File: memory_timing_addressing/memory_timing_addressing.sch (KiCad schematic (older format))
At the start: 1 part, among them P1 DIN_41612_128P

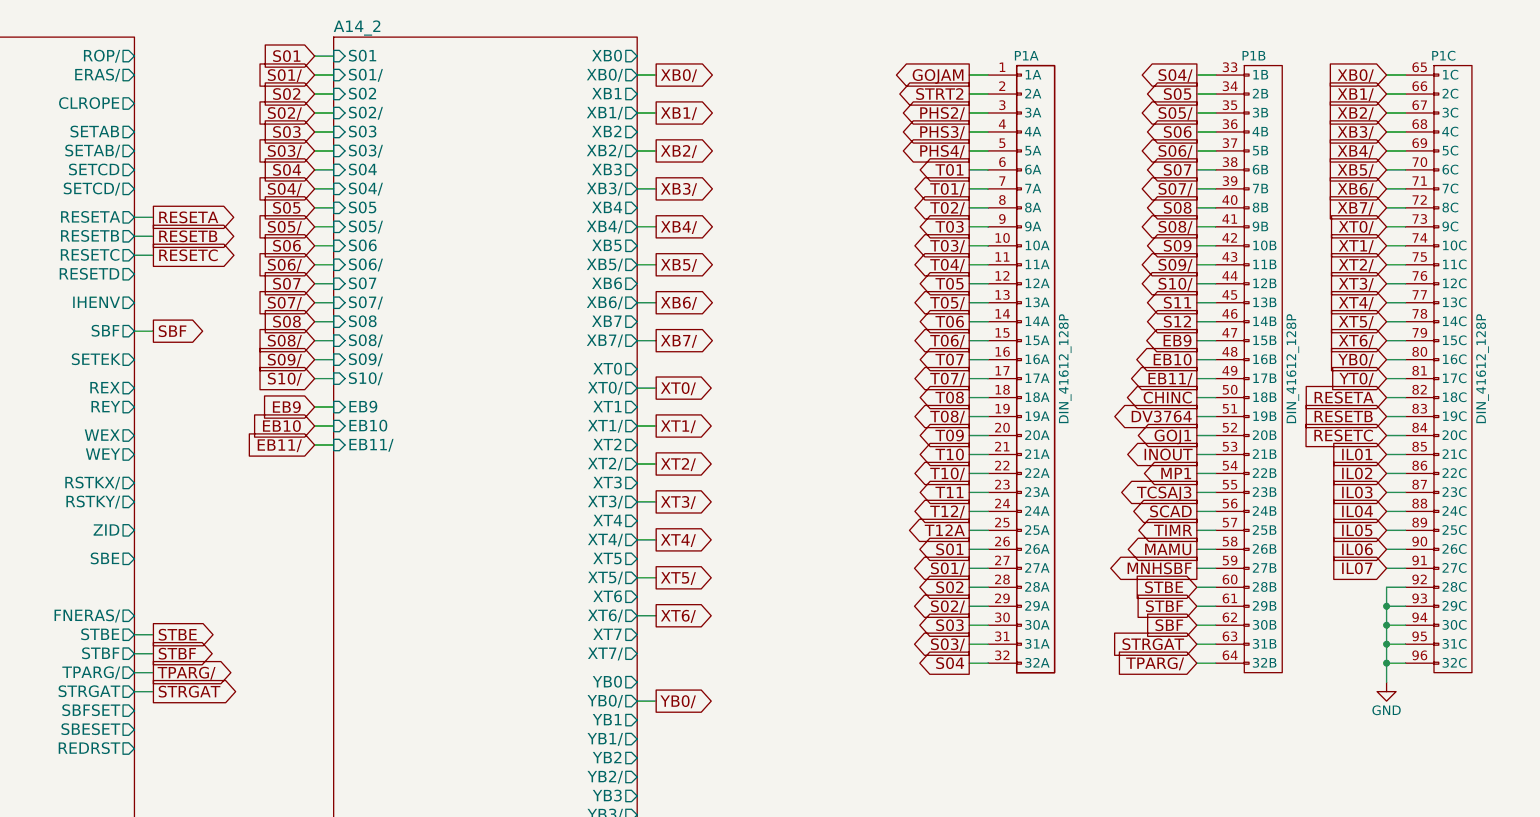
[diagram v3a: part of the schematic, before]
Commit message: Updated fixed memory model, plus various bugfixes
Rope memory control signals are now decoded much earlier in the cycle to
determine the target address, allowing slower memory devices (such as
the EPCS on the DE0 Nano) enough time to load their data.

The bugfixes are mostly wiring errors discovered by debugging lockups in
when running Colossus 237 -- all were causing the ST2 pulse to not
occur, so errors that *don't* prevent ST2 from happening very well might
be present in the instructions that have been fixed.

The computer now gets through the initialization code and enters an
infinite loop when attempting to invoke the interpeter, due to the lack
of erasable memory.
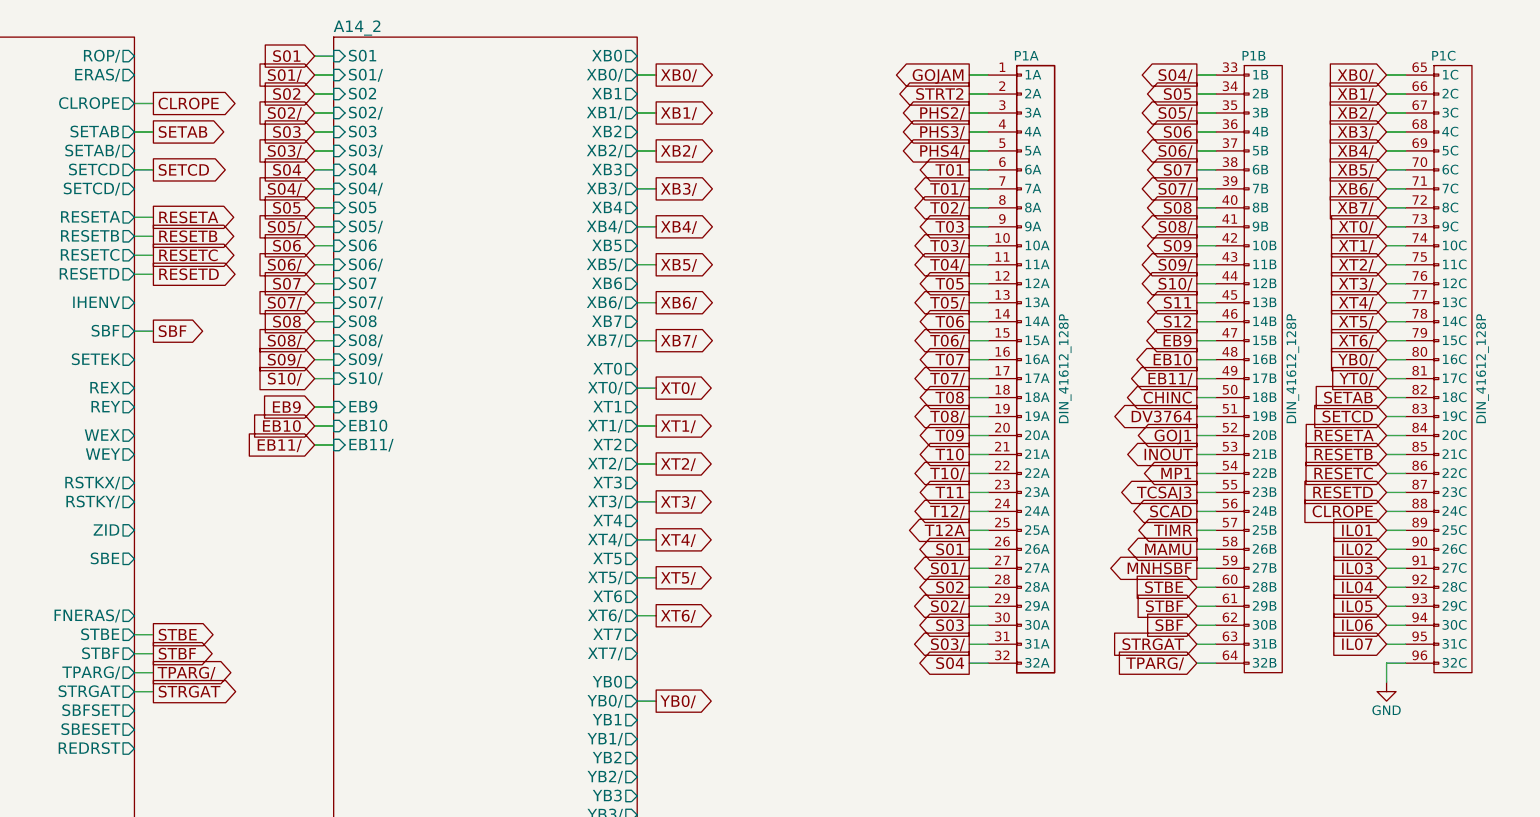
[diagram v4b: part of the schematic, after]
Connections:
- net GND: no longer P1.92 (28C), P1.93 (29C), P1.94 (30C), P1.95 (31C)
- net IL01: now also P1.89 (25C); no longer P1.85 (21C)
- net IL02: now also P1.90 (26C); no longer P1.86 (22C)
- net IL03: now also P1.91 (27C); no longer P1.87 (23C)
- net IL04: now also P1.92 (28C); no longer P1.88 (24C)
- net IL05: now also P1.93 (29C); no longer P1.89 (25C)
- net IL06: now also P1.94 (30C); no longer P1.90 (26C)
- net IL07: now also P1.95 (31C); no longer P1.91 (27C)
- net RESETA: now also P1.84 (20C); no longer P1.82 (18C)
- net RESETB: now also P1.85 (21C); no longer P1.83 (19C)
- net RESETC: now also P1.86 (22C); no longer P1.84 (20C)
- new net CLROPE: P1.88 (24C)
- new net RESETD: P1.87 (23C)
- new net SETAB: P1.82 (18C)
- new net SETCD: P1.83 (19C)
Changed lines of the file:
@@
 $EndComp
 Wire Wire Line
-	9450 4100 9550 4100
-Wire Wire Line
-	9450 4200 9550 4200
-Connection ~ 9450 4200
-Wire Wire Line
-	9450 4300 9550 4300
-Connection ~ 9450 4300
-Wire Wire Line
-	9450 4400 9550 4400
-Connection ~ 9450 4400
-Wire Wire Line
 	9450 4500 9550 4500
-Connection ~ 9450 4500
 $Comp
 L GND #PWR01
@@
 RESETC
 Wire Wire Line
-	9550 3100 9450 3100
-Text GLabel 9450 3100 0    60   Input ~ 0
-RESETA
-Wire Wire Line
-	9550 3200 9450 3200
-Text GLabel 9450 3200 0    60   Input ~ 0
-RESETB
-Wire Wire Line
 	9550 3300 9450 3300
 Text GLabel 9450 3300 0    60   Input ~ 0
+RESETA
+Wire Wire Line
+	9550 3400 9450 3400
+Text GLabel 9450 3400 0    60   Input ~ 0
+RESETB
+Wire Wire Line
+	9550 3500 9450 3500
+Text GLabel 9450 3500 0    60   Input ~ 0
 RESETC
 Wire Wire Line
@@
 IL07
 Wire Wire Line
-	9550 3400 9450 3400
-Text GLabel 9450 3400 0    60   Input ~ 0
-IL01
-Wire Wire Line
-	9550 3500 9450 3500
-Text GLabel 9450 3500 0    60   Input ~ 0
-IL02
-Wire Wire Line
-	9550 3600 9450 3600
-Text GLabel 9450 3600 0    60   Input ~ 0
-IL03
-Wire Wire Line
-	9550 3700 9450 3700
-Text GLabel 9450 3700 0    60   Input ~ 0
-IL04
-Wire Wire Line
 	9550 3800 9450 3800
 Text GLabel 9450 3800 0    60   Input ~ 0
-IL05
+IL01
 Wire Wire Line
 	9550 3900 9450 3900
 Text GLabel 9450 3900 0    60   Input ~ 0
-IL06
+IL02
 Wire Wire Line
 	9550 4000 9450 4000
 Text GLabel 9450 4000 0    60   Input ~ 0
+IL03
+Wire Wire Line
+	9550 4100 9450 4100
+Text GLabel 9450 4100 0    60   Input ~ 0
+IL04
+Wire Wire Line
+	9550 4200 9450 4200
+Text GLabel 9450 4200 0    60   Input ~ 0
+IL05
+Wire Wire Line
+	9550 4300 9450 4300
+Text GLabel 9450 4300 0    60   Input ~ 0
+IL06
+Wire Wire Line
+	9550 4400 9450 4400
+Text GLabel 9450 4400 0    60   Input ~ 0
 IL07
 Wire Wire Line
@@
 SBF
 Wire Wire Line
-	9450 4100 9450 4600
-Wire Wire Line
 	8550 4300 8450 4300
 Text GLabel 8450 4300 0    60   Input ~ 0
 SBF
+Wire Wire Line
+	2850 2450 2950 2450
+Text GLabel 2950 2450 2    60   Output ~ 0
+RESETD
+Wire Wire Line
+	9550 3600 9450 3600
+Text GLabel 9450 3600 0    60   Input ~ 0
+RESETD
+Wire Wire Line
+	9550 3100 9450 3100
+Text GLabel 9450 3100 0    60   Input ~ 0
+SETAB
+Wire Wire Line
+	9550 3200 9450 3200
+Text GLabel 9450 3200 0    60   Input ~ 0
+SETCD
+Wire Wire Line
+	2850 1700 2950 1700
+Text GLabel 2950 1700 2    60   Output ~ 0
+SETAB
+Wire Wire Line
+	2850 1900 2950 1900
+Text GLabel 2950 1900 2    60   Output ~ 0
+SETCD
+Wire Wire Line
+	2850 1550 2950 1550
+Text GLabel 2950 1550 2    60   Output ~ 0
+CLROPE
+Wire Wire Line
+	9450 4500 9450 4600
+Wire Wire Line
+	9550 3700 9450 3700
+Text GLabel 9450 3700 0    60   Input ~ 0
+CLROPE
 $EndSCHEMATC

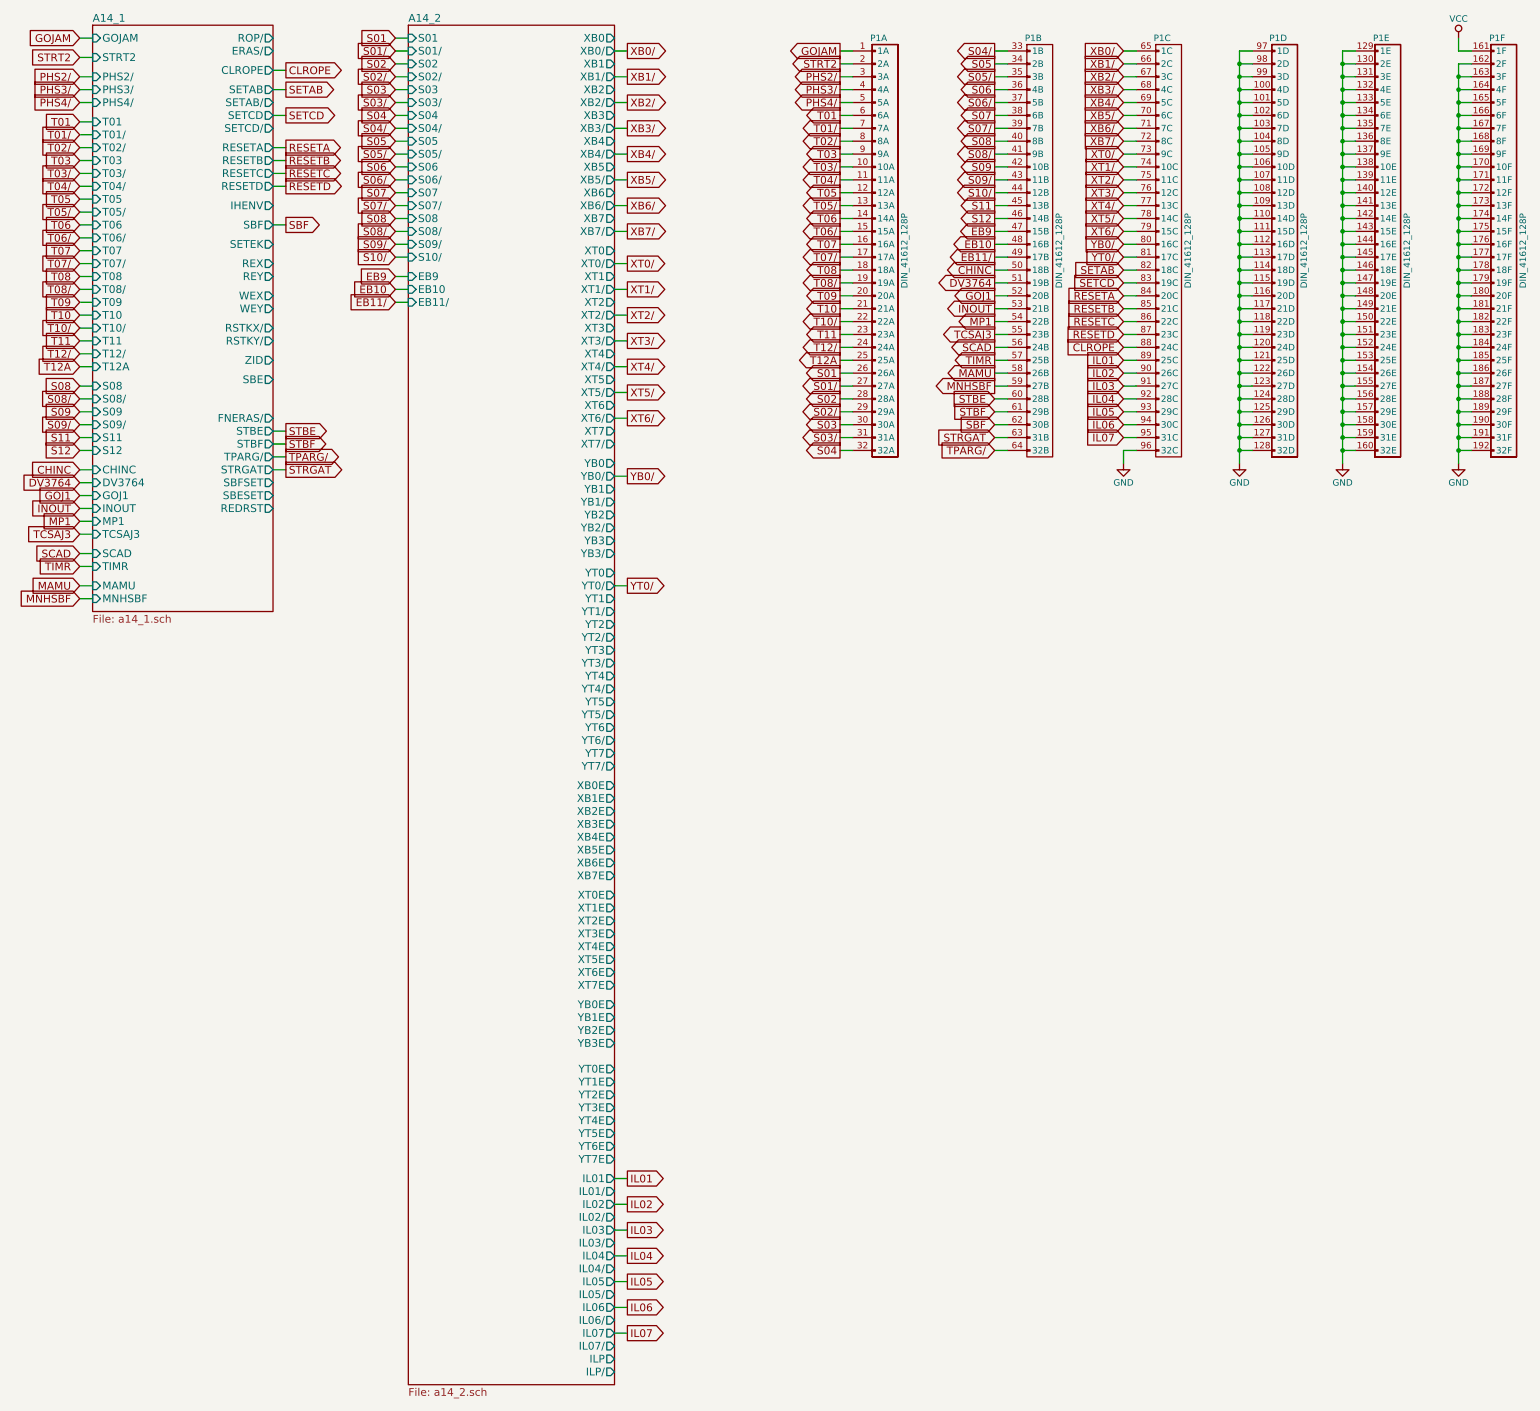
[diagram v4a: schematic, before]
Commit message: Added erasable memory, and fixed lots of random wiring errors.
I decided to go with a 16-bit-wide MRAM chip -- I had  no idea
until I started researching RAM options how technologically
similar MRAM is to core memory. The datasheet diagrams look like
they're straight out of the AGC documentation!

There's a slight inaccuracy in this implementation worth mentioning.
Like fixed memory, I've wired the sense amplifier outputs directly up
to the tristate data output pins of the MRAM chip. But because the
data lines are bidirectional, data being written into RAM will show up
on the sense lines, and go straight into the ungated G register. Since
G is what's being written out, this doesn't matter 99% of the time, but
if there's an overflow condition in G (I don't even know if this is
possible), the bit 16 will be copied over bit 16, and the overflow
condition will be lost. I'll keep an eye out to see if anything relies
on G not changing after the write cycle is complete.

With erasable memory introduced, the computer now theoretically supports
all programs that don't use I/O or interrupts. I've started running
the VirtualAGC validation program, and have been fixing random errors
uncovered by failing self-tests.
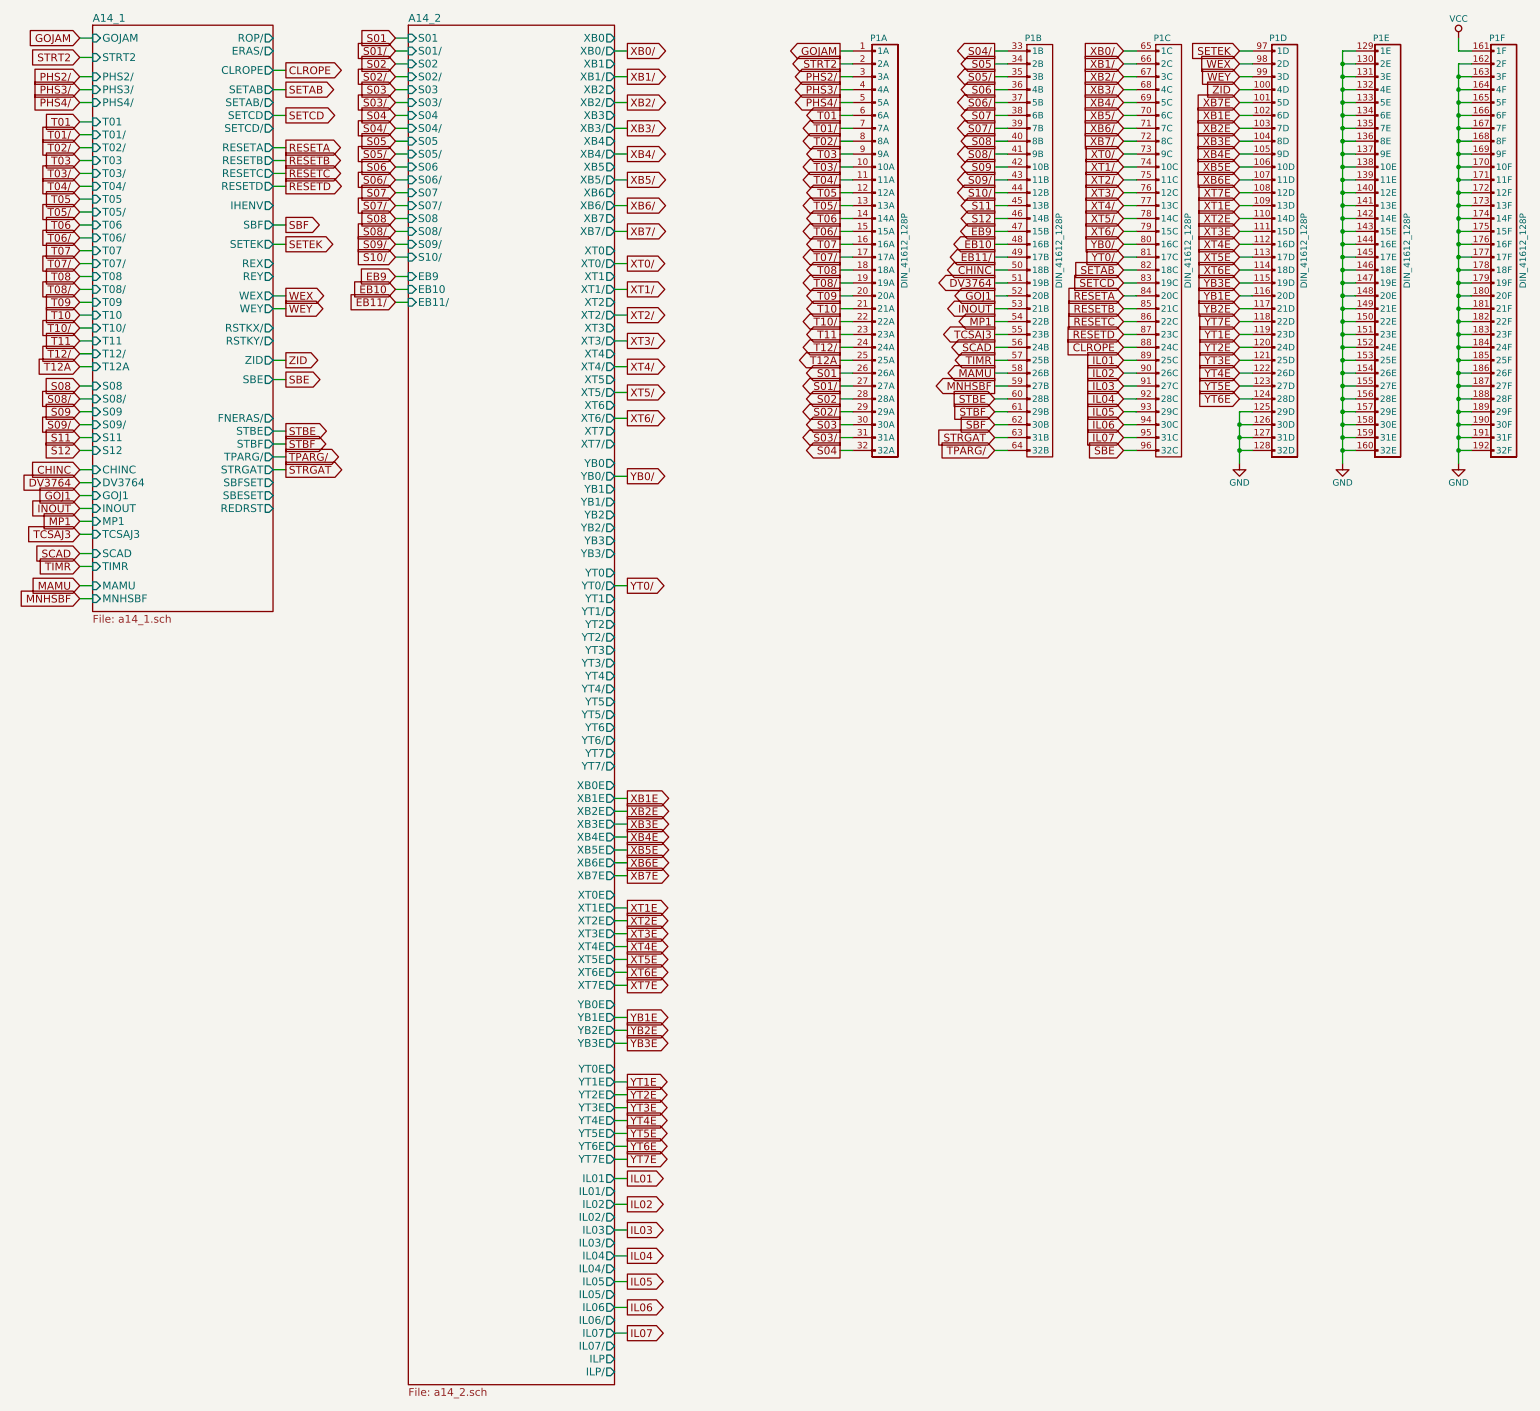
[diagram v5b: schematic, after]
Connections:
- net GND: no longer P1.100 (4D), P1.101 (5D), P1.102 (6D), P1.103 (7D), P1.104 (8D), P1.105 (9D), P1.106 (10D), P1.107 (11D), P1.108 (12D), P1.109 (13D), P1.110 (14D), P1.111 (15D), P1.112 (16D), P1.113 (17D), P1.114 (18D), P1.115 (19D), P1.116 (20D), P1.117 (21D), P1.118 (22D), P1.119 (23D), P1.120 (24D), P1.121 (25D), P1.122 (26D), P1.123 (27D), P1.124 (28D), P1.96 (32C), P1.97 (1D), P1.98 (2D), P1.99 (3D)
- new net SBE: P1.96 (32C)
- new net SETEK: P1.97 (1D)
- new net WEX: P1.98 (2D)
- new net WEY: P1.99 (3D)
- new net XB1E: P1.102 (6D)
- new net XB2E: P1.103 (7D)
- new net XB3E: P1.104 (8D)
- new net XB4E: P1.105 (9D)
- new net XB5E: P1.106 (10D)
- new net XB6E: P1.107 (11D)
- new net XB7E: P1.101 (5D)
- new net XT1E: P1.109 (13D)
- new net XT2E: P1.110 (14D)
- new net XT3E: P1.111 (15D)
- new net XT4E: P1.112 (16D)
- new net XT5E: P1.113 (17D)
- new net XT6E: P1.114 (18D)
- new net XT7E: P1.108 (12D)
- new net YB1E: P1.116 (20D)
- new net YB2E: P1.117 (21D)
- new net YB3E: P1.115 (19D)
- new net YT1E: P1.119 (23D)
- new net YT2E: P1.120 (24D)
- new net YT3E: P1.121 (25D)
- new net YT4E: P1.122 (26D)
- new net YT5E: P1.123 (27D)
- new net YT6E: P1.124 (28D)
- new net YT7E: P1.118 (22D)
- new net ZID: P1.100 (4D)
